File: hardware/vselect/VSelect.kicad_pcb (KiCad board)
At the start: 2 copper layers, 15.4 x 10 mm, 10 parts, among them U1 TPS2113PW

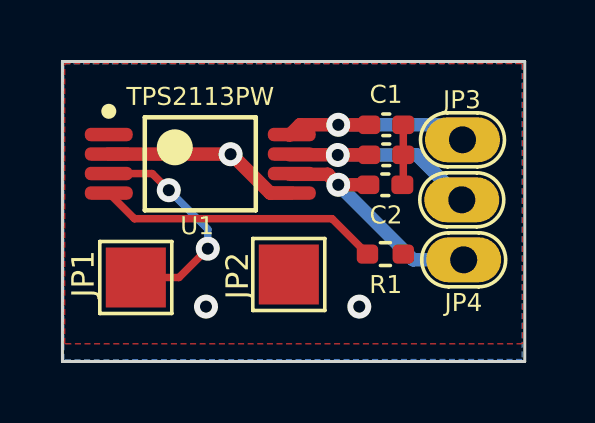
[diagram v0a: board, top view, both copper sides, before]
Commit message: Fix Vselect PCB
5V and 3.3V were backwards on the headers to connect to the main PCB.

Note: If you already ordered the PCB it still can be used, just install it upside down.
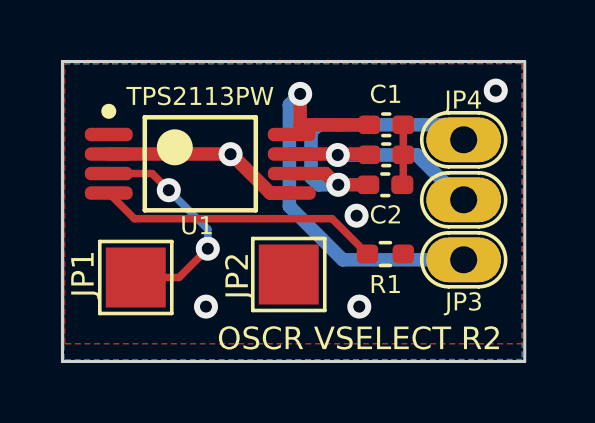
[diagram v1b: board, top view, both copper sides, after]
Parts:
- moved JP3 4.00 mm to (40.3, 22.9)
- moved JP4 4.00 mm to (40.3, 18.9)
- moved JP5 0.06 mm to (40.3, 20.9)
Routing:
- net +3.3V: track 7.72 -> 13.8 mm
- net +5V: track 7.99 -> 10.6 mm
- net GND: vias 3 -> 5
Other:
- board text added: "OSCR VSELECT R2"
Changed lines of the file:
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@@
   )
   (footprint "Personal:Vpower-Switch-Pad" (layer "F.Cu")
-    (at 40.29 18.89)
-    (property "Sheetfile" "VSelect.kicad_sch")
-    (property "Sheetname" "")
-    (attr smd)
-    (fp_text reference "JP3" (at -0.02 -0.23 unlocked) (layer "F.SilkS")
+    (at 40.33 22.89)
+    (property "Sheetfile" "VSelect.kicad_sch")
+    (property "Sheetname" "")
+    (attr smd)
+    (fp_text reference "JP3" (at 0.01 2.51 unlocked) (layer "F.SilkS")
       (effects (font (size 0.6 0.6) (thickness 0.125)))
     )
@@
   )
   (footprint "Personal:Vpower-Switch-Pad" (layer "F.Cu")
-    (at 40.266635 20.89)
+    (at 40.33 20.89)
     (property "Sheetfile" "VSelect.kicad_sch")
     (property "Sheetname" "")
@@
   )
   (footprint "Personal:Vpower-Switch-Pad" (layer "F.Cu")
-    (at 40.33 22.89)
-    (property "Sheetfile" "VSelect.kicad_sch")
-    (property "Sheetname" "")
-    (attr smd)
-    (fp_text reference "JP4" (at -0.01 2.53 unlocked) (layer "F.SilkS")
+    (at 40.33 18.89)
+    (property "Sheetfile" "VSelect.kicad_sch")
+    (property "Sheetname" "")
+    (attr smd)
+    (fp_text reference "JP4" (at -0.01 -0.22 unlocked) (layer "F.SilkS")
       (effects (font (size 0.6 0.6) (thickness 0.125)))
     )
@@
   )
   (gr_rect (start 42.365 27.38) (end 26.955 17.38) (layer "Edge.Cuts") (width 0.1) (fill none))
+  (gr_text "OSCR VSELECT R2" (at 36.86 26.62) (layer "F.SilkS")
+    (effects (font (size 0.75 0.75) (thickness 0.15)))
+  )
   (segment (start 38.3175 19.49) (end 38.3175 21.4575) (width 0.25) (layer "F.Cu") (net 1))
   (segment (start 33.88137 21.765002) (end 34.600002 21.765002) (width 0.45) (layer "F.Cu") (net 1))
@@
   (via (at 31.74 25.55) (size 0.8) (drill 0.4) (layers "F.Cu" "B.Cu") (free) (net 1))
   (via (at 36.85 25.55) (size 0.8) (drill 0.4) (layers "F.Cu" "B.Cu") (free) (net 1))
+  (via (at 36.76 22.52) (size 0.8) (drill 0.4) (layers "F.Cu" "B.Cu") (free) (net 1))
   (via (at 32.56 20.47) (size 0.8) (drill 0.4) (layers "F.Cu" "B.Cu") (free) (net 1))
-  (segment (start 34.875 19.49) (end 34.525001 19.839999) (width 0.45) (layer "F.Cu") (net 2))
+  (via (at 41.4 18.35) (size 0.8) (drill 0.4) (layers "F.Cu" "B.Cu") (free) (net 1))
+  (segment (start 34.88 18.46) (end 34.88 19.535003) (width 0.45) (layer "F.Cu") (net 2))
   (segment (start 37.1825 19.49) (end 36.15 19.49) (width 0.45) (layer "F.Cu") (net 2))
   (segment (start 36.15 19.49) (end 34.875 19.49) (width 0.45) (layer "F.Cu") (net 2))
-  (via (at 36.15 19.49) (size 0.8) (drill 0.4) (layers "F.Cu" "B.Cu") (free) (net 2))
-  (segment (start 36.15 19.49) (end 39.79 19.49) (width 0.45) (layer "B.Cu") (net 2))
-  (segment (start 39.9 19.6) (end 40.3 20) (width 0.45) (layer "B.Cu") (net 2))
-  (segment (start 39.79 19.49) (end 40.29 19.99) (width 0.45) (layer "B.Cu") (net 2))
-  (segment (start 34.525001 21.139999) (end 35.799999 21.139999) (width 0.45) (layer "F.Cu") (net 3))
+  (via (at 34.88 18.46) (size 0.8) (drill 0.4) (layers "F.Cu" "B.Cu") (free) (net 2))
+  (segment (start 34.52 22.21) (end 34.52 18.82) (width 0.45) (layer "B.Cu") (net 2))
+  (segment (start 40.33 23.99) (end 36.3 23.99) (width 0.45) (layer "B.Cu") (net 2))
+  (segment (start 36.3 23.99) (end 34.52 22.21) (width 0.45) (layer "B.Cu") (net 2))
+  (segment (start 34.52 18.82) (end 34.88 18.46) (width 0.45) (layer "B.Cu") (net 2))
+  (segment (start 35.725666 21.115001) (end 36.100665 21.49) (width 0.45) (layer "F.Cu") (net 3))
+  (segment (start 34.600002 21.115001) (end 35.725666 21.115001) (width 0.45) (layer "F.Cu") (net 3))
   (segment (start 37.15 21.49) (end 36.15 21.49) (width 0.45) (layer "F.Cu") (net 3))
-  (segment (start 35.799999 21.139999) (end 36.15 21.49) (width 0.45) (layer "F.Cu") (net 3))
+  (segment (start 36.100665 21.49) (end 36.15 21.49) (width 0.45) (layer "F.Cu") (net 3))
   (via (at 36.15 21.49) (size 0.8) (drill 0.4) (layers "F.Cu" "B.Cu") (free) (net 3))
-  (segment (start 38.65 23.99) (end 40.33 23.99) (width 0.45) (layer "B.Cu") (net 3))
-  (segment (start 36.15 21.49) (end 38.65 23.99) (width 0.45) (layer "B.Cu") (net 3))
-  (segment (start 34.525001 20.49) (end 37.1825 20.49) (width 0.45) (layer "F.Cu") (net 4))
+  (segment (start 35.24 19.74) (end 35.49 19.49) (width 0.45) (layer "B.Cu") (net 3))
+  (segment (start 35.49 19.49) (end 39.83 19.49) (width 0.45) (layer "B.Cu") (net 3))
+  (segment (start 35.49 21.49) (end 35.24 21.24) (width 0.45) (layer "B.Cu") (net 3))
+  (segment (start 39.83 19.49) (end 40.33 19.99) (width 0.45) (layer "B.Cu") (net 3))
+  (segment (start 35.24 21.24) (end 35.24 19.74) (width 0.45) (layer "B.Cu") (net 3))
+  (segment (start 36.15 21.49) (end 35.49 21.49) (width 0.45) (layer "B.Cu") (net 3))
+  (segment (start 37.157502 20.465002) (end 37.1825 20.49) (width 0.45) (layer "F.Cu") (net 4))
+  (segment (start 34.549999 20.465002) (end 37.157502 20.465002) (width 0.45) (layer "F.Cu") (net 4))
   (via (at 36.132031 20.496061) (size 0.8) (drill 0.4) (layers "F.Cu" "B.Cu") (free) (net 4))
   (segment (start 36.132031 20.496061) (end 38.772696 20.496061) (width 0.45) (layer "B.Cu") (net 4))
